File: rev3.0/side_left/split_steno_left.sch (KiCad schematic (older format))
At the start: 31 parts, among them J1 USB_B, J2 Audio-Jack-4, P1 TC2030-IDC, SW1 SW_Push, SW10 SW_Push, SW11 SW_Push, SW12 SW_Push, SW13 SW_Push, SW14 SW_Push, SW15 SW_Push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

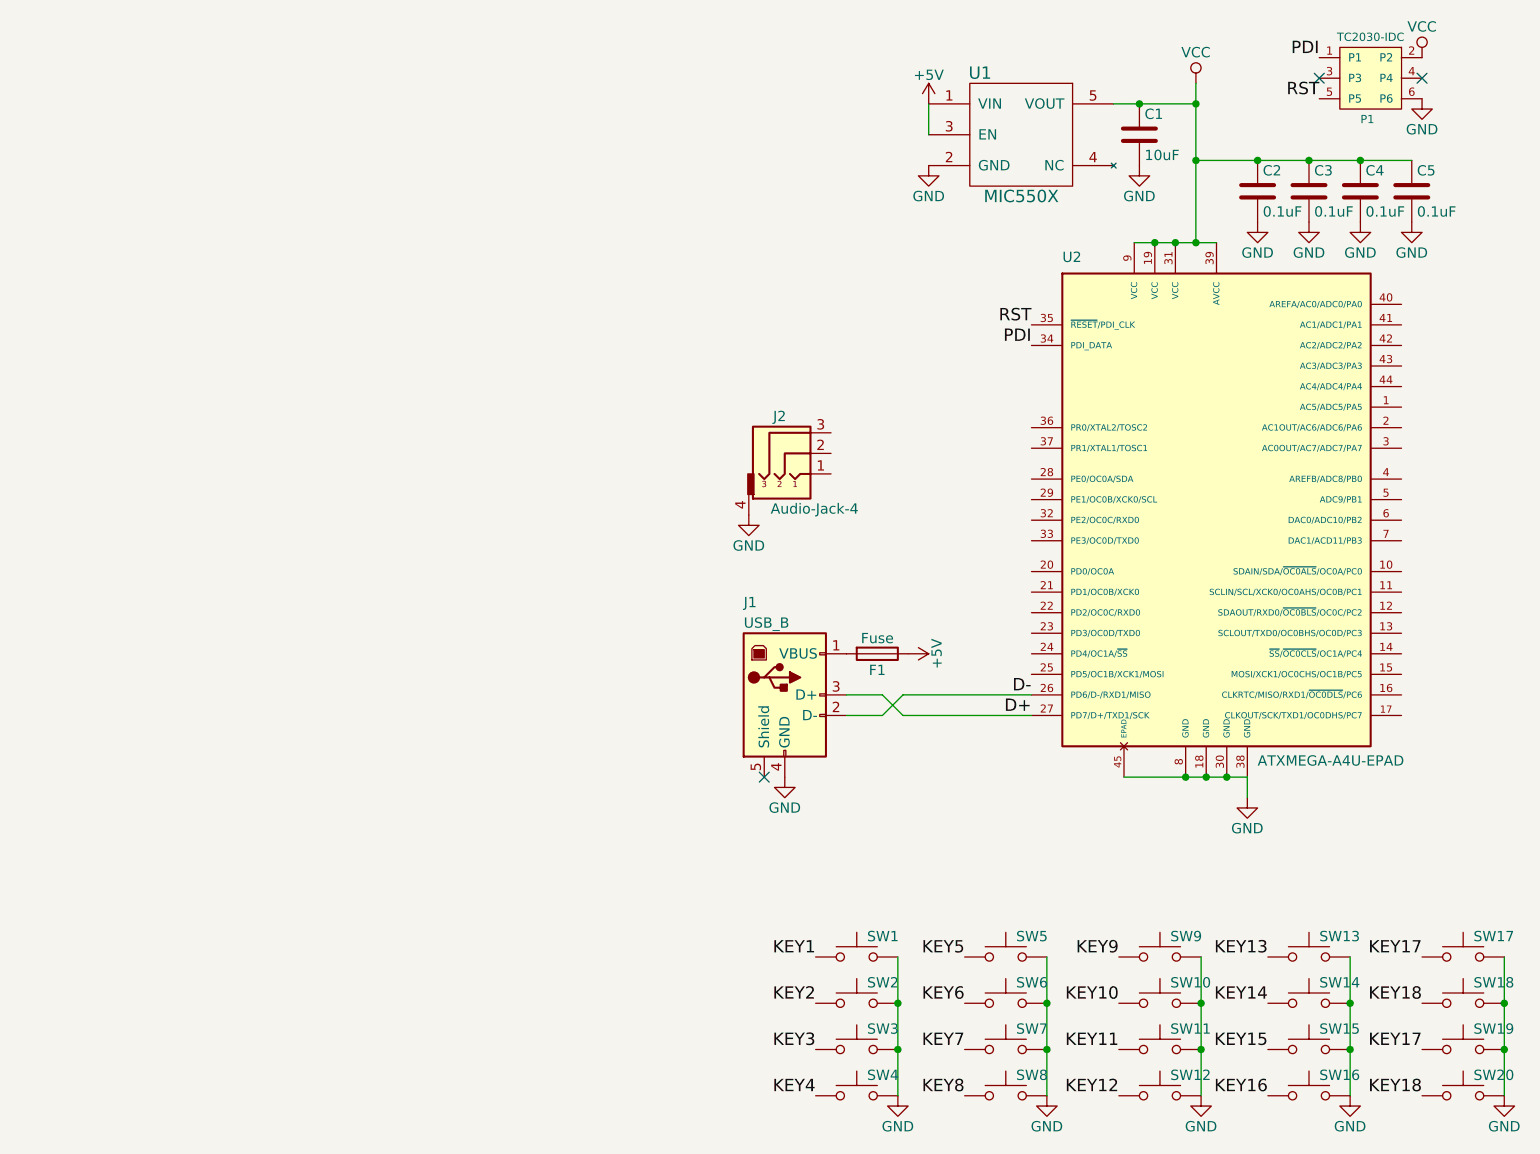
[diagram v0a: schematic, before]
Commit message: added edge cuts, and mounting holes
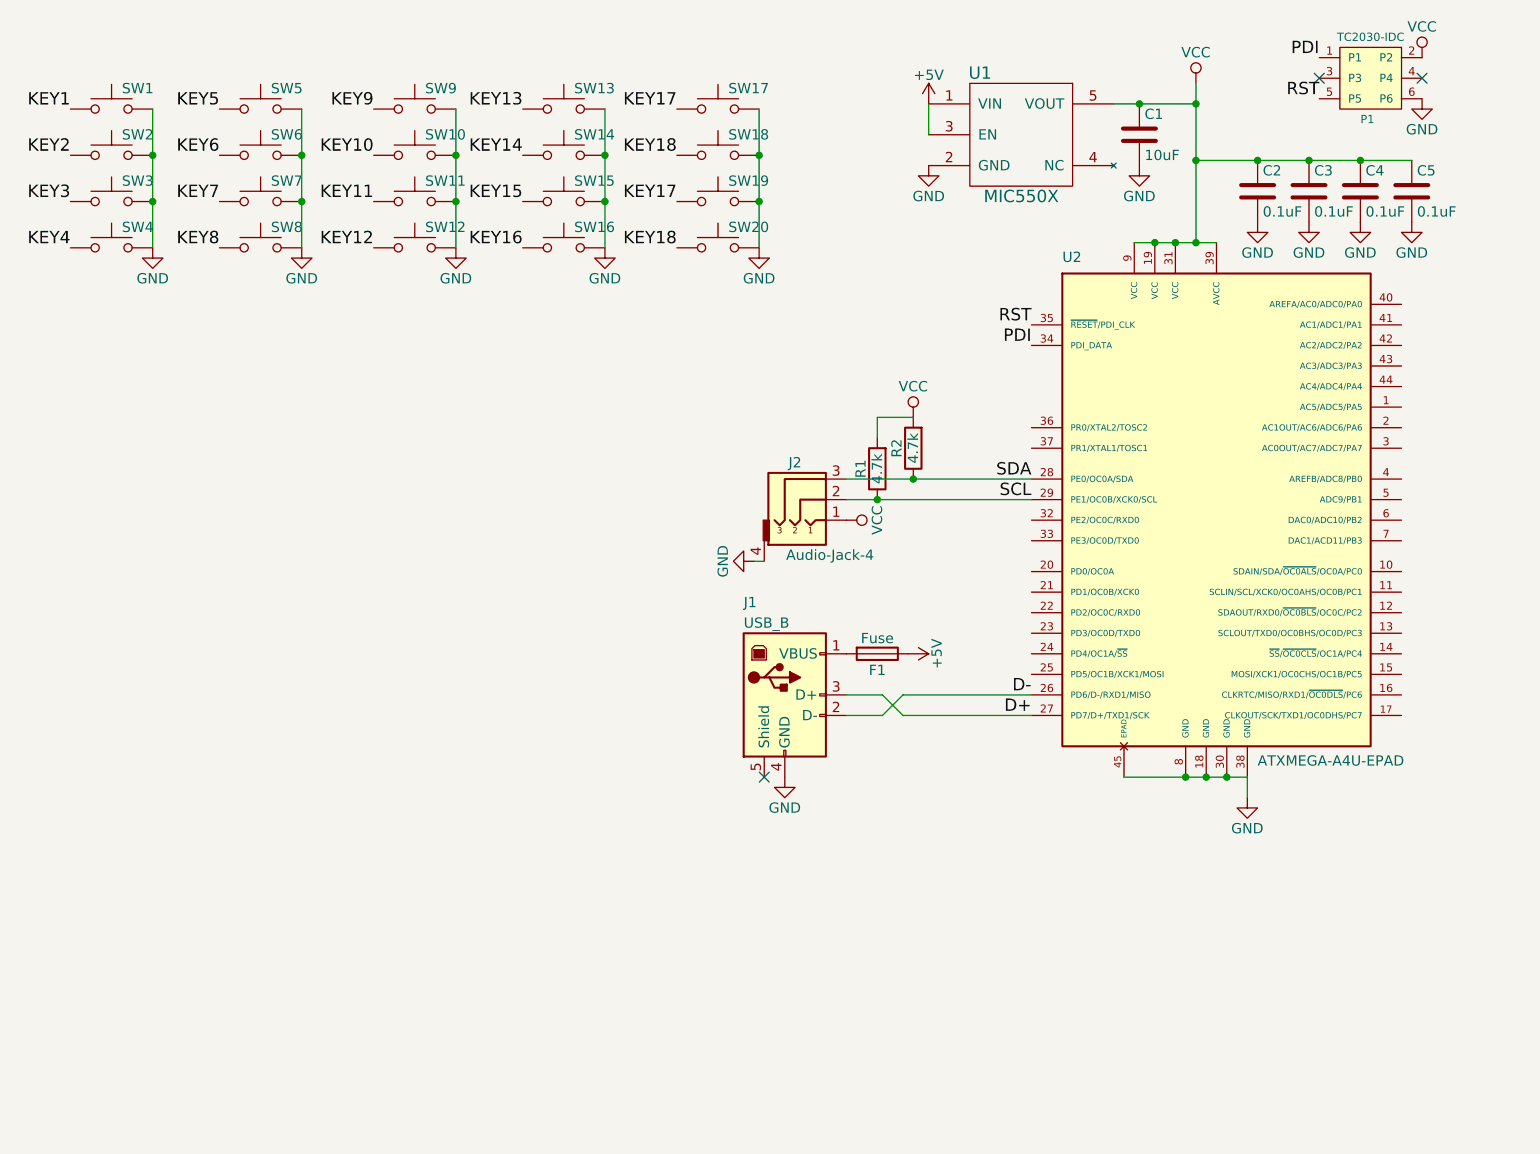
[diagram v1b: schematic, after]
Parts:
- added R1, R2: 4.7k, Resistors_SMD:R_0805_HandSoldering, symbol R
- SW19, SW20: footprint MX_Alps_Hybrid:MX-2U-ReversedStabilizers-NoLED -> MX_Alps_Hybrid:MX-2U-NoLED
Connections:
- net VCC: now also J2.1, R1.2, R2.2
- net SCL: now reaches J2.2
- net SCL: now also U2.29 (PE1/OC0B/XCK0/SCL), R1.1
- net SDA: now reaches J2.3
- net SDA: now also U2.28 (PE0/OC0A/SDA), R2.1
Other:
- moved on the sheet: J2, SW1, SW10, SW11, SW12, SW13, SW14, SW15, SW16, SW17, SW18, SW19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

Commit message: things (i forgot what changed)
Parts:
- C1, C2, C3, C4, C5: footprint Capacitors_SMD:C_0805_HandSoldering -> Capacitors_SMD:C_0603_HandSoldering
- R1, R2: footprint Resistors_SMD:R_0805_HandSoldering -> Resistors_SMD:R_0603_HandSoldering
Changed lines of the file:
@@
 F 0 "C1" H 8525 1450 50  0000 L CNN
 F 1 "10uF" H 8525 1250 50  0000 L CNN
-F 2 "Capacitors_SMD:C_0805_HandSoldering" H 8538 1200 50  0001 C CNN
+F 2 "Capacitors_SMD:C_0603_HandSoldering" H 8538 1200 50  0001 C CNN
 F 3 "" H 8500 1350 50  0001 C CNN
 	1    8500 1350
@@
 F 0 "C2" H 9100 1725 50  0000 L CNN
 F 1 "0.1uF" H 9100 1525 50  0000 L CNN
-F 2 "Capacitors_SMD:C_0805_HandSoldering" H 9113 1475 50  0001 C CNN
+F 2 "Capacitors_SMD:C_0603_HandSoldering" H 9113 1475 50  0001 C CNN
 F 3 "" H 9075 1625 50  0001 C CNN
 	1    9075 1625
@@
 F 0 "C3" H 9350 1725 50  0000 L CNN
 F 1 "0.1uF" H 9350 1525 50  0000 L CNN
-F 2 "Capacitors_SMD:C_0805_HandSoldering" H 9363 1475 50  0001 C CNN
+F 2 "Capacitors_SMD:C_0603_HandSoldering" H 9363 1475 50  0001 C CNN
 F 3 "" H 9325 1625 50  0001 C CNN
 	1    9325 1625
@@
 F 0 "C4" H 9600 1725 50  0000 L CNN
 F 1 "0.1uF" H 9600 1525 50  0000 L CNN
-F 2 "Capacitors_SMD:C_0805_HandSoldering" H 9613 1475 50  0001 C CNN
+F 2 "Capacitors_SMD:C_0603_HandSoldering" H 9613 1475 50  0001 C CNN
 F 3 "" H 9575 1625 50  0001 C CNN
 	1    9575 1625
@@
 F 0 "C5" H 9850 1725 50  0000 L CNN
 F 1 "0.1uF" H 9850 1525 50  0000 L CNN
-F 2 "Capacitors_SMD:C_0805_HandSoldering" H 9863 1475 50  0001 C CNN
+F 2 "Capacitors_SMD:C_0603_HandSoldering" H 9863 1475 50  0001 C CNN
 F 3 "" H 9825 1625 50  0001 C CNN
 	1    9825 1625
@@
 F 0 "R1" V 7305 2975 50  0000 C CNN
 F 1 "4.7k" V 7225 2975 50  0000 C CNN
-F 2 "Resistors_SMD:R_0805_HandSoldering" V 7155 2975 50  0001 C CNN
+F 2 "Resistors_SMD:R_0603_HandSoldering" V 7155 2975 50  0001 C CNN
 F 3 "" H 7225 2975 50  0001 C CNN
 	1    7225 2975
@@
 F 0 "R2" V 7480 2875 50  0000 C CNN
 F 1 "4.7k" V 7400 2875 50  0000 C CNN
-F 2 "Resistors_SMD:R_0805_HandSoldering" V 7330 2875 50  0001 C CNN
+F 2 "Resistors_SMD:R_0603_HandSoldering" V 7330 2875 50  0001 C CNN
 F 3 "" H 7400 2875 50  0001 C CNN
 	1    7400 2875
@@
 Connection ~ 7225 3125
 $Comp
-L VCC #PWR?
+L VCC #PWR020
 U 1 1 5AFFE474
 P 7400 2725
-F 0 "#PWR?" H 7400 2575 50  0001 C CNN
+F 0 "#PWR020" H 7400 2575 50  0001 C CNN
 F 1 "VCC" H 7400 2875 50  0000 C CNN
 F 2 "" H 7400 2725 50  0001 C CNN
@@
 $EndComp
 $Comp
-L VCC #PWR?
+L VCC #PWR021
 U 1 1 5AFFE4E2
 P 7075 3225
-F 0 "#PWR?" H 7075 3075 50  0001 C CNN
+F 0 "#PWR021" H 7075 3075 50  0001 C CNN
 F 1 "VCC" H 7075 3375 50  0000 C CNN
 F 2 "" H 7075 3225 50  0001 C CNN
